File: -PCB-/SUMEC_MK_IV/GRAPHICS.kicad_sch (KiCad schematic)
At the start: 0 parts

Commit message: MK_IV update
Power supp sheet done, mechanical sheet almost done, some changes, updates etc.
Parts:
- added R16: R, sumec-remote_library:purosidenegative, symbol Device:R
- added R17: R, sumec-smdV2_library:SPS LOGO, symbol Device:R
- added R18: R, sumec-remote_library:boi, symbol Device:R
- added R19: R, sumec-smdV2_library:Logo, symbol Device:R
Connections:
- no-connect marks 0 -> 8
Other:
- note added: "ART"

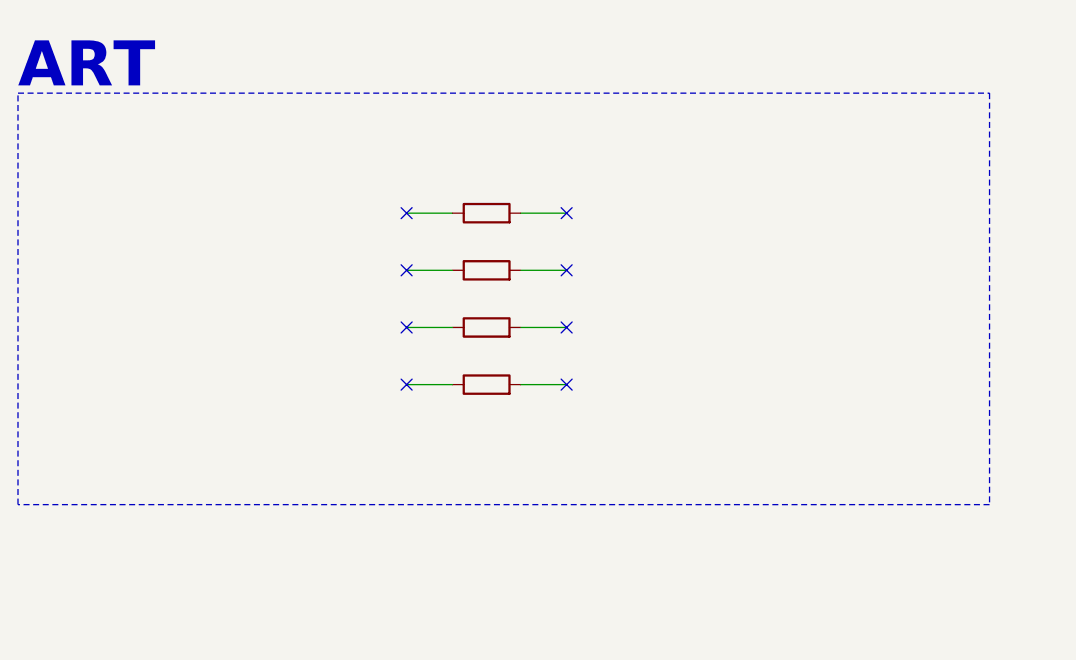
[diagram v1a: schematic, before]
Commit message: MKIV major update
Updated everything, custom symbol for ESP32, MCU sheet done, new test points added, motor control revision.

all left is to clean it up a bit
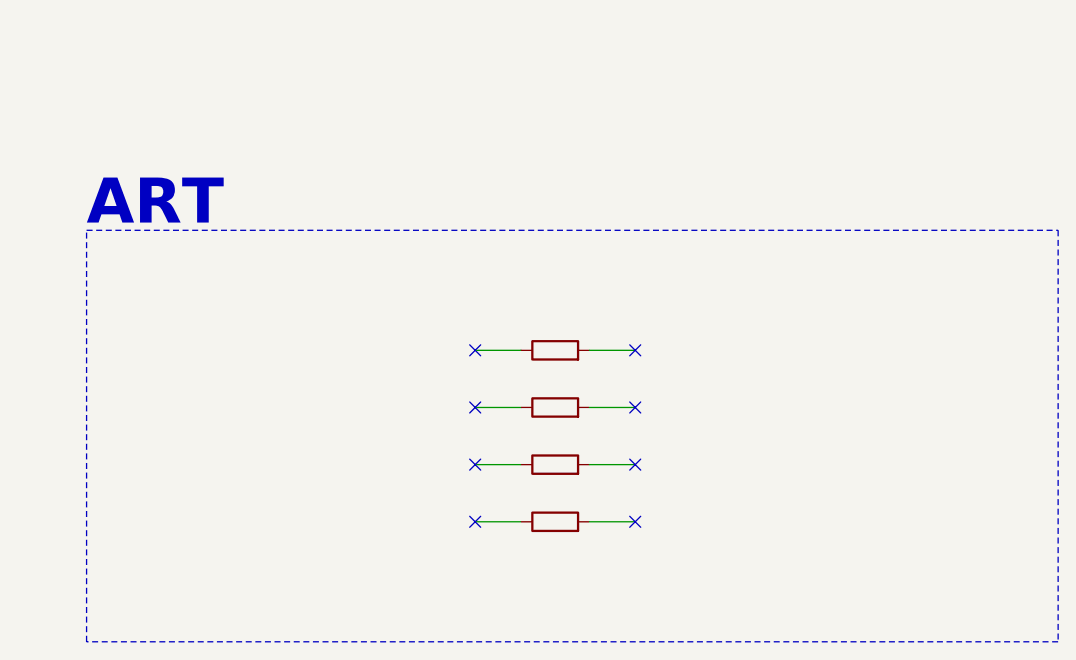
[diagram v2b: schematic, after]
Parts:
- renumbered R16 to R27, R17 to R28, R18 to R29, R19 to R30
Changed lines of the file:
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@@
 	(title_block
 		(title "SUMEC_MK_IV")
-		(date "2024-07-01")
+		(date "2024-07-15")
+		(rev "v3.0.0")
 		(company "SPS NA PROSEKU")
-		(comment 1 "SAVVA POPOV")
-	)
-	(no_connect
-		(at 148.59 87.63)
-	)
-	(no_connect
-		(at 148.59 74.93)
-	)
-	(no_connect
-		(at 130.81 74.93)
-	)
-	(no_connect
-		(at 148.59 81.28)
-	)
-	(no_connect
-		(at 148.59 93.98)
-	)
-	(no_connect
-		(at 130.81 81.28)
-	)
-	(no_connect
-		(at 130.81 87.63)
-	)
-	(no_connect
-		(at 130.81 93.98)
-	)
-	(wire
-		(pts
-			(xy 130.81 87.63) (xy 135.89 87.63)
-		)
-		(stroke
-			(width 0)
-			(type default)
-		)
-	)
-	(wire
-		(pts
-			(xy 148.59 74.93) (xy 143.51 74.93)
-		)
-		(stroke
-			(width 0)
-			(type default)
-		)
-	)
-	(wire
-		(pts
-			(xy 148.59 87.63) (xy 143.51 87.63)
-		)
-		(stroke
-			(width 0)
-			(type default)
-		)
-	)
-	(wire
-		(pts
-			(xy 148.59 81.28) (xy 143.51 81.28)
-		)
-		(stroke
-			(width 0)
-			(type default)
-		)
-	)
-	(wire
-		(pts
-			(xy 148.59 93.98) (xy 143.51 93.98)
-		)
-		(stroke
-			(width 0)
-			(type default)
-		)
-	)
-	(wire
-		(pts
-			(xy 130.81 81.28) (xy 135.89 81.28)
-		)
-		(stroke
-			(width 0)
-			(type default)
-		)
-	)
-	(wire
-		(pts
-			(xy 130.81 74.93) (xy 135.89 74.93)
-		)
-		(stroke
-			(width 0)
-			(type default)
-		)
-	)
-	(wire
-		(pts
-			(xy 130.81 93.98) (xy 135.89 93.98)
+		(comment 1 "Made in Prague, Czech Republic")
+		(comment 2 "CONTACT: Savva Popov, menmenson09@gmail.com, +420 605 570 366")
+		(comment 3 "Made by Bismarx aka MenMenson")
+		(comment 4 "SUMEC MK IV aka SMD-V3 board")
+	)
+	(no_connect
+		(at 156.21 102.87)
+	)
+	(no_connect
+		(at 156.21 90.17)
+	)
+	(no_connect
+		(at 138.43 90.17)
+	)
+	(no_connect
+		(at 156.21 96.52)
+	)
+	(no_connect
+		(at 156.21 109.22)
+	)
+	(no_connect
+		(at 138.43 96.52)
+	)
+	(no_connect
+		(at 138.43 102.87)
+	)
+	(no_connect
+		(at 138.43 109.22)
+	)
+	(wire
+		(pts
+			(xy 138.43 102.87) (xy 143.51 102.87)
+		)
+		(stroke
+			(width 0)
+			(type default)
+		)
+	)
+	(wire
+		(pts
+			(xy 156.21 90.17) (xy 151.13 90.17)
+		)
+		(stroke
+			(width 0)
+			(type default)
+		)
+	)
+	(wire
+		(pts
+			(xy 156.21 102.87) (xy 151.13 102.87)
+		)
+		(stroke
+			(width 0)
+			(type default)
+		)
+	)
+	(wire
+		(pts
+			(xy 156.21 96.52) (xy 151.13 96.52)
+		)
+		(stroke
+			(width 0)
+			(type default)
+		)
+	)
+	(wire
+		(pts
+			(xy 156.21 109.22) (xy 151.13 109.22)
+		)
+		(stroke
+			(width 0)
+			(type default)
+		)
+	)
+	(wire
+		(pts
+			(xy 138.43 96.52) (xy 143.51 96.52)
+		)
+		(stroke
+			(width 0)
+			(type default)
+		)
+	)
+	(wire
+		(pts
+			(xy 138.43 90.17) (xy 143.51 90.17)
+		)
+		(stroke
+			(width 0)
+			(type default)
+		)
+	)
+	(wire
+		(pts
+			(xy 138.43 109.22) (xy 143.51 109.22)
 		)
 		(stroke
@@
 	)
 	(rectangle
-		(start 87.63 61.595)
-		(end 195.58 107.315)
+		(start 95.25 76.835)
+		(end 203.2 122.555)
 		(stroke
 			(width 0)
@@
 	(text "ART"
 		(exclude_from_sim no)
-		(at 87.63 61.595 0)
+		(at 95.25 76.835 0)
 		(effects
 			(font
@@
 	(symbol
 		(lib_id "Device:R")
-		(at 139.7 74.93 90)
+		(at 147.32 90.17 90)
 		(unit 1)
 		(exclude_from_sim no)
@@
 		(dnp no)
 		(fields_autoplaced yes)
-		(property "Reference" "R16"
-			(at 139.7 68.58 90)
+		(property "Reference" "R27"
+			(at 147.32 83.82 90)
 			(effects
 				(font
@@
 		)
 		(property "Value" "R"
-			(at 139.7 71.12 90)
+			(at 147.32 86.36 90)
 			(effects
 				(font
@@
 		)
 		(property "Footprint" "sumec-remote_library:purosidenegative"
-			(at 139.7 76.708 90)
+			(at 147.32 91.948 90)
 			(effects
 				(font
@@
 		)
 		(property "Datasheet" "~"
-			(at 139.7 74.93 0)
+			(at 147.32 90.17 0)
 			(effects
 				(font
@@
 		)
 		(property "Description" "Resistor"
-			(at 139.7 74.93 0)
+			(at 147.32 90.17 0)
 			(effects
 				(font
@@
 			(project "SUMEC_MK_IV"
 				(path "/900bd7ac-cdf9-4a2f-8b1f-2c21e3760046/ebfdffb9-be38-48cc-bdc4-81d227bad184"
-					(reference "R16")
+					(reference "R27")
 					(unit 1)
 				)
@@
 	(symbol
 		(lib_id "Device:R")
-		(at 139.7 81.28 90)
+		(at 147.32 96.52 90)
 		(unit 1)
 		(exclude_from_sim no)
@@
 		(dnp no)
 		(fields_autoplaced yes)
-		(property "Reference" "R17"
-			(at 139.7 74.93 90)
+		(property "Reference" "R28"
+			(at 147.32 90.17 90)
 			(effects
 				(font
@@
 		)
 		(property "Value" "R"
-			(at 139.7 77.47 90)
+			(at 147.32 92.71 90)
 			(effects
 				(font
@@
 		)
 		(property "Footprint" "sumec-smdV2_library:SPS LOGO"
-			(at 139.7 83.058 90)
+			(at 147.32 98.298 90)
 			(effects
 				(font
@@
 		)
 		(property "Datasheet" "~"
-			(at 139.7 81.28 0)
+			(at 147.32 96.52 0)
 			(effects
 				(font
@@
 		)
 		(property "Description" "Resistor"
-			(at 139.7 81.28 0)
+			(at 147.32 96.52 0)
 			(effects
 				(font
@@
 			(project "SUMEC_MK_IV"
 				(path "/900bd7ac-cdf9-4a2f-8b1f-2c21e3760046/ebfdffb9-be38-48cc-bdc4-81d227bad184"
-					(reference "R17")
+					(reference "R28")
 					(unit 1)
 				)
@@
 	(symbol
 		(lib_id "Device:R")
-		(at 139.7 87.63 90)
+		(at 147.32 102.87 90)
 		(unit 1)
 		(exclude_from_sim no)
@@
 		(dnp no)
 		(fields_autoplaced yes)
-		(property "Reference" "R18"
-			(at 139.7 81.28 90)
+		(property "Reference" "R29"
+			(at 147.32 96.52 90)
 			(effects
 				(font
@@
 		)
 		(property "Value" "R"
-			(at 139.7 83.82 90)
+			(at 147.32 99.06 90)
 			(effects
 				(font
@@
 		)
 		(property "Footprint" "sumec-remote_library:boi"
-			(at 139.7 89.408 90)
+			(at 147.32 104.648 90)
 			(effects
 				(font
@@
 		)
 		(property "Datasheet" "~"
-			(at 139.7 87.63 0)
+			(at 147.32 102.87 0)
 			(effects
 				(font
@@
 		)
 		(property "Description" "Resistor"
-			(at 139.7 87.63 0)
+			(at 147.32 102.87 0)
 			(effects
 				(font
@@
 			(project "SUMEC_MK_IV"
 				(path "/900bd7ac-cdf9-4a2f-8b1f-2c21e3760046/ebfdffb9-be38-48cc-bdc4-81d227bad184"
-					(reference "R18")
+					(reference "R29")
 					(unit 1)
 				)
@@
 	(symbol
 		(lib_id "Device:R")
-		(at 139.7 93.98 90)
+		(at 147.32 109.22 90)
 		(unit 1)
 		(exclude_from_sim no)
@@
 		(dnp no)
 		(fields_autoplaced yes)
-		(property "Reference" "R19"
-			(at 139.7 87.63 90)
+		(property "Reference" "R30"
+			(at 147.32 102.87 90)
 			(effects
 				(font
@@
 		)
 		(property "Value" "R"
-			(at 139.7 90.17 90)
+			(at 147.32 105.41 90)
 			(effects
 				(font
@@
 		)
 		(property "Footprint" "sumec-smdV2_library:Logo"
-			(at 139.7 95.758 90)
+			(at 147.32 110.998 90)
 			(effects
 				(font
@@
 		)
 		(property "Datasheet" "~"
-			(at 139.7 93.98 0)
+			(at 147.32 109.22 0)
 			(effects
 				(font
@@
 		)
 		(property "Description" "Resistor"
-			(at 139.7 93.98 0)
+			(at 147.32 109.22 0)
 			(effects
 				(font
@@
 			(project "SUMEC_MK_IV"
 				(path "/900bd7ac-cdf9-4a2f-8b1f-2c21e3760046/ebfdffb9-be38-48cc-bdc4-81d227bad184"
-					(reference "R19")
+					(reference "R30")
 					(unit 1)
 				)

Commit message: v3.0.9 SUMEC PCB
Ufff, so, basically a full rewrite of the PCB, check it our its pretty sick, I think
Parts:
- renumbered R27 to R20, R28 to R21, R29 to R22, R30 to R23
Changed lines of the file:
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@@
 	(title_block
 		(title "SUMEC_MK_IV")
-		(date "2024-07-15")
-		(rev "v3.0.0")
+		(date "2024-08-05")
+		(rev "v3.0.9")
 		(company "SPS NA PROSEKU")
 		(comment 1 "Made in Prague, Czech Republic")
@@
 		(dnp no)
 		(fields_autoplaced yes)
-		(property "Reference" "R27"
+		(property "Reference" "R20"
 			(at 147.32 83.82 90)
 			(effects
@@
 			(project "SUMEC_MK_IV"
 				(path "/900bd7ac-cdf9-4a2f-8b1f-2c21e3760046/ebfdffb9-be38-48cc-bdc4-81d227bad184"
-					(reference "R27")
+					(reference "R20")
 					(unit 1)
 				)
@@
 		(dnp no)
 		(fields_autoplaced yes)
-		(property "Reference" "R28"
+		(property "Reference" "R21"
 			(at 147.32 90.17 90)
 			(effects
@@
 			(project "SUMEC_MK_IV"
 				(path "/900bd7ac-cdf9-4a2f-8b1f-2c21e3760046/ebfdffb9-be38-48cc-bdc4-81d227bad184"
-					(reference "R28")
+					(reference "R21")
 					(unit 1)
 				)
@@
 		(dnp no)
 		(fields_autoplaced yes)
-		(property "Reference" "R29"
+		(property "Reference" "R22"
 			(at 147.32 96.52 90)
 			(effects
@@
 			(project "SUMEC_MK_IV"
 				(path "/900bd7ac-cdf9-4a2f-8b1f-2c21e3760046/ebfdffb9-be38-48cc-bdc4-81d227bad184"
-					(reference "R29")
+					(reference "R22")
 					(unit 1)
 				)
@@
 		(dnp no)
 		(fields_autoplaced yes)
-		(property "Reference" "R30"
+		(property "Reference" "R23"
 			(at 147.32 102.87 90)
 			(effects
@@
 			(project "SUMEC_MK_IV"
 				(path "/900bd7ac-cdf9-4a2f-8b1f-2c21e3760046/ebfdffb9-be38-48cc-bdc4-81d227bad184"
-					(reference "R30")
+					(reference "R23")
 					(unit 1)
 				)

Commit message: DRC Hell fix
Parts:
- removed R20: R, sumec-remote_library:purosidenegative, symbol Device:R
- removed R21: R, sumec-smdV2_library:SPS LOGO, symbol Device:R
- removed R22: R, sumec-remote_library:boi, symbol Device:R
- removed R23: R, sumec-smdV2_library:Logo, symbol Device:R
- added TP5: TestPoint, sumec_graphic:SPS_LOGO_IMG, symbol Connector:TestPoint
- added TP6: TestPoint, sumec_graphic:SUMEC_LOGO_IMG, symbol Connector:TestPoint
- added TP7: TestPoint, sumec_graphic:ULTRAKILL_IMG, symbol Connector:TestPoint
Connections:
- new net: TP5.1, TP6.1, TP7.1
- no-connect marks 8 -> 1

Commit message: Silkscreen, added "touch", updated PDF.
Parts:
- added TP8: TestPoint, sumec_graphic:ME_FR_IMG, symbol Connector:TestPoint
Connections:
- net at TP5.1, TP6.1, TP7.1: now also TP8.1
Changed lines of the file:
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@@
+	)
+	(junction
+		(at 137.16 97.79)
+		(diameter 0)
+		(color 0 0 0 0)
 	)
 	(junction
@@
 	(wire
 		(pts
+			(xy 140.97 97.79) (xy 137.16 97.79)
+		)
+		(stroke
+			(width 0)
+			(type default)
+		)
+	)
+	(wire
+		(pts
 			(xy 133.35 97.79) (xy 137.16 97.79)
+		)
+		(stroke
+			(width 0)
+			(type default)
+		)
+	)
+	(wire
+		(pts
+			(xy 140.97 95.25) (xy 140.97 97.79)
 		)
 		(stroke
@@
 		)
 	)
+	(symbol
+		(lib_id "Connector:TestPoint")
+		(at 140.97 95.25 0)
+		(unit 1)
+		(exclude_from_sim no)
+		(in_bom yes)
+		(on_board yes)
+		(dnp no)
+		(fields_autoplaced yes)
+		(property "Reference" "TP8"
+			(at 143.51 90.6779 0)
+			(effects
+				(font
+					(size 1.27 1.27)
+				)
+				(justify left)
+				(hide yes)
+			)
+		)
+		(property "Value" "TestPoint"
+			(at 143.51 93.2179 0)
+			(effects
+				(font
+					(size 1.27 1.27)
+				)
+				(justify left)
+				(hide yes)
+			)
+		)
+		(property "Footprint" "sumec_graphic:ME_FR_IMG"
+			(at 146.05 95.25 0)
+			(effects
+				(font
+					(size 1.27 1.27)
+				)
+				(hide yes)
+			)
+		)
+		(property "Datasheet" "~"
+			(at 146.05 95.25 0)
+			(effects
+				(font
+					(size 1.27 1.27)
+				)
+				(hide yes)
+			)
+		)
+		(property "Description" "test point"
+			(at 140.97 95.25 0)
+			(effects
+				(font
+					(size 1.27 1.27)
+				)
+				(hide yes)
+			)
+		)
+		(pin "1"
+		)
+		(instances
+			(project "SUMEC_MK_IV"
+				(path "/900bd7ac-cdf9-4a2f-8b1f-2c21e3760046/ebfdffb9-be38-48cc-bdc4-81d227bad184"
+					(reference "TP8")
+					(unit 1)
+				)
+			)
+		)
+	)

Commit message: BOM + silkscreen
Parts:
- added TP10: TestPoint, sumec_graphic:FREEFALL_IMG, symbol Connector:TestPoint
- added TP9: TestPoint, sumec_graphic:SUMEC_INST_IMG, symbol Connector:TestPoint
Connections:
- net at TP5.1, TP6.1, TP7.1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: now also TP10.1, TP9.1
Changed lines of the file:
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@@
+	)
+	(junction
+		(at 140.97 97.79)
+		(diameter 0)
+		(color 0 0 0 0)
 	)
 	(junction
 		(at 133.35 97.79)
+		(diameter 0)
+		(color 0 0 0 0)
+	)
+	(junction
+		(at 144.78 97.79)
 		(diameter 0)
 		(color 0 0 0 0)
@@
 	(wire
 		(pts
+			(xy 144.78 97.79) (xy 148.59 97.79)
+		)
+		(stroke
+			(width 0)
+			(type default)
+		)
+	)
+	(wire
+		(pts
 			(xy 137.16 95.25) (xy 137.16 97.79)
 		)
@@
 	(wire
 		(pts
+			(xy 144.78 95.25) (xy 144.78 97.79)
+		)
+		(stroke
+			(width 0)
+			(type default)
+		)
+	)
+	(wire
+		(pts
 			(xy 129.54 97.79) (xy 133.35 97.79)
 		)
@@
 	(wire
 		(pts
+			(xy 144.78 97.79) (xy 140.97 97.79)
+		)
+		(stroke
+			(width 0)
+			(type default)
+		)
+	)
+	(wire
+		(pts
 			(xy 140.97 95.25) (xy 140.97 97.79)
+		)
+		(stroke
+			(width 0)
+			(type default)
+		)
+	)
+	(wire
+		(pts
+			(xy 148.59 97.79) (xy 148.59 95.25)
 		)
 		(stroke
@@
 		)
 	)
+	(symbol
+		(lib_id "Connector:TestPoint")
+		(at 144.78 95.25 0)
+		(unit 1)
+		(exclude_from_sim no)
+		(in_bom yes)
+		(on_board yes)
+		(dnp no)
+		(fields_autoplaced yes)
+		(property "Reference" "TP9"
+			(at 147.32 90.6779 0)
+			(effects
+				(font
+					(size 1.27 1.27)
+				)
+				(justify left)
+				(hide yes)
+			)
+		)
+		(property "Value" "TestPoint"
+			(at 147.32 93.2179 0)
+			(effects
+				(font
+					(size 1.27 1.27)
+				)
+				(justify left)
+				(hide yes)
+			)
+		)
+		(property "Footprint" "sumec_graphic:SUMEC_INST_IMG"
+			(at 149.86 95.25 0)
+			(effects
+				(font
+					(size 1.27 1.27)
+				)
+				(hide yes)
+			)
+		)
+		(property "Datasheet" "~"
+			(at 149.86 95.25 0)
+			(effects
+				(font
+					(size 1.27 1.27)
+				)
+				(hide yes)
+			)
+		)
+		(property "Description" "test point"
+			(at 144.78 95.25 0)
+			(effects
+				(font
+					(size 1.27 1.27)
+				)
+				(hide yes)
+			)
+		)
+		(pin "1"
+		)
+		(instances
+			(project "SUMEC_MK_IV"
+				(path "/900bd7ac-cdf9-4a2f-8b1f-2c21e3760046/ebfdffb9-be38-48cc-bdc4-81d227bad184"
+					(reference "TP9")
+					(unit 1)
+				)
+			)
+		)
+	)
+	(symbol
+		(lib_id "Connector:TestPoint")
+		(at 148.59 95.25 0)
+		(unit 1)
+		(exclude_from_sim no)
+		(in_bom yes)
+		(on_board yes)
+		(dnp no)
+		(fields_autoplaced yes)
+		(property "Reference" "TP10"
+			(at 151.13 90.6779 0)
+			(effects
+				(font
+					(size 1.27 1.27)
+				)
+				(justify left)
+				(hide yes)
+			)
+		)
+		(property "Value" "TestPoint"
+			(at 151.13 93.2179 0)
+			(effects
+				(font
+					(size 1.27 1.27)
+				)
+				(justify left)
+				(hide yes)
+			)
+		)
+		(property "Footprint" "sumec_graphic:FREEFALL_IMG"
+			(at 153.67 95.25 0)
+			(effects
+				(font
+					(size 1.27 1.27)
+				)
+				(hide yes)
+			)
+		)
+		(property "Datasheet" "~"
+			(at 153.67 95.25 0)
+			(effects
+				(font
+					(size 1.27 1.27)
+				)
+				(hide yes)
+			)
+		)
+		(property "Description" "test point"
+			(at 148.59 95.25 0)
+			(effects
+				(font
+					(size 1.27 1.27)
+				)
+				(hide yes)
+			)
+		)
+		(pin "1"
+		)
+		(instances
+			(project "SUMEC_MK_IV"
+				(path "/900bd7ac-cdf9-4a2f-8b1f-2c21e3760046/ebfdffb9-be38-48cc-bdc4-81d227bad184"
+					(reference "TP10")
+					(unit 1)
+				)
+			)
+		)
+	)

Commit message: different qr, linktree
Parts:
- TP9: footprint sumec_graphic:SUMEC_INST_IMG -> sumec_graphic:SUMEC_QR_IMG
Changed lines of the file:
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@@
 			)
 		)
-		(property "Footprint" "sumec_graphic:SUMEC_INST_IMG"
+		(property "Footprint" "sumec_graphic:SUMEC_QR_IMG"
 			(at 149.86 95.25 0)
 			(effects

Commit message: Free fall IMG
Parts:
- TP10: footprint sumec_graphic:FREEFALL_IMG -> sumec_graphic:FREFALL_COMIC_IMG
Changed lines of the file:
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@@
 			)
 		)
-		(property "Footprint" "sumec_graphic:FREEFALL_IMG"
+		(property "Footprint" "sumec_graphic:FREFALL_COMIC_IMG"
 			(at 153.67 95.25 0)
 			(effects
